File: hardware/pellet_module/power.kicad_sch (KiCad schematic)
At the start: 28 parts, among them J22 Barrel_Jack_Switch, U8 TPS561201, U9 TPS565208

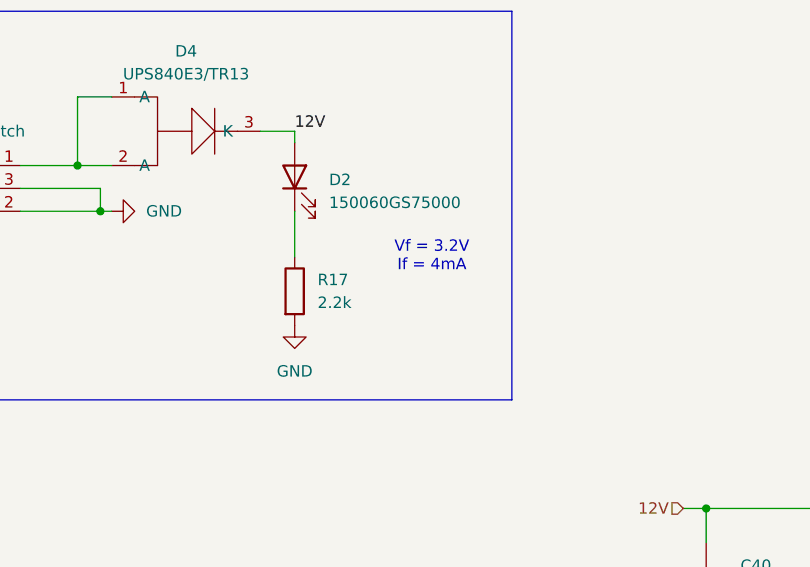
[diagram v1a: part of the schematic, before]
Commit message: reduce power LED brightness
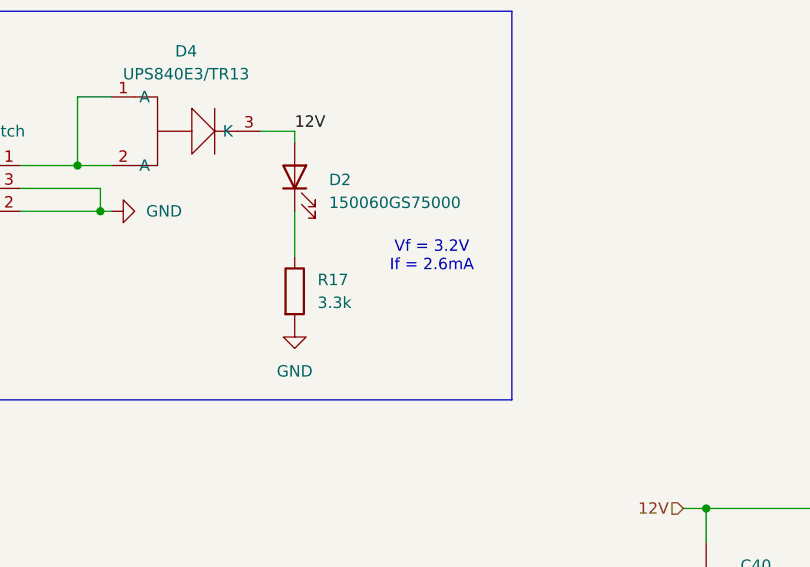
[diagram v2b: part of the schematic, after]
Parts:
- R17: value 2.2k -> 3.3k; LCSC C4190 -> C22978; MPN 0603WAF2201T5E -> 0603WAF3301T5E
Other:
- note added: "Vf = 3.2V If = 2.6mA"
- note removed: "Vf = 3.2V If = 4mA"
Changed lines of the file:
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@@
 		)
 	)
-	(text "Vf = 3.2V\nIf = 4mA"
+	(text "Vf = 3.2V\nIf = 2.6mA"
 		(exclude_from_sim no)
 		(at 78.74 45.72 0)
@@
 			)
 		)
-		(property "Value" "2.2k"
+		(property "Value" "3.3k"
 			(at 66.04 50.7999 0)
 			(effects
@@
 			)
 		)
-		(property "MPN" "0603WAF2201T5E"
+		(property "MPN" "0603WAF3301T5E"
 			(at 63.5 49.53 0)
 			(effects
@@
 			)
 		)
-		(property "LCSC" "C4190"
+		(property "LCSC" "C22978"
 			(at 63.5 49.53 0)
 			(effects

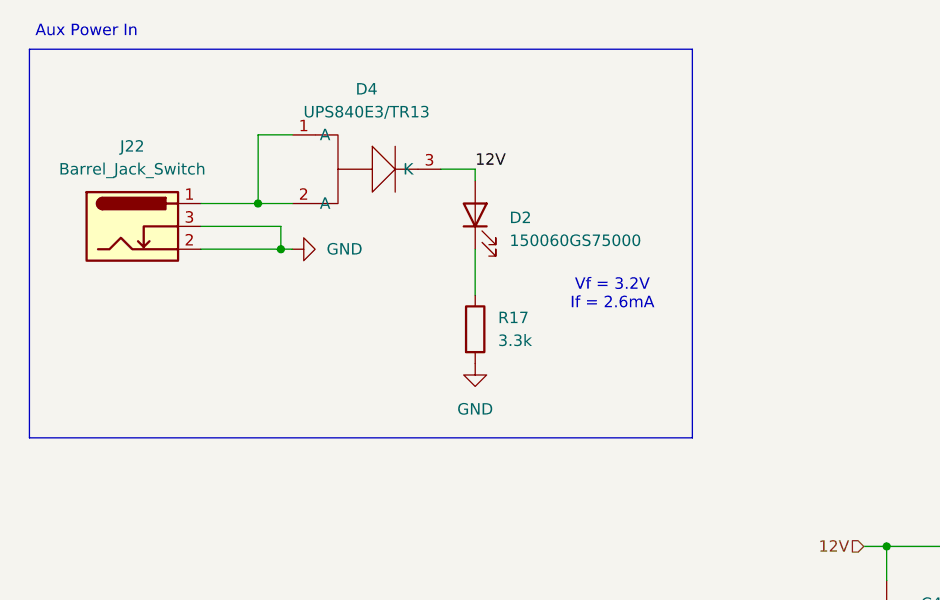
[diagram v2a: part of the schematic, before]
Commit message: add test points to schematic
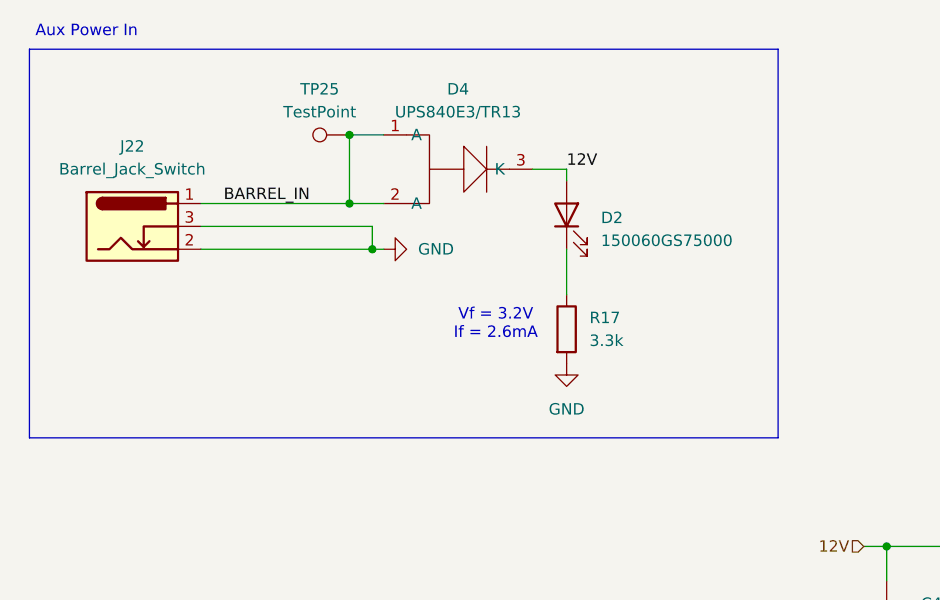
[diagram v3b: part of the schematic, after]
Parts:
- added TP25: TestPoint, TestPoint:TestPoint_Pad_1.0x1.0mm, symbol Connector:TestPoint
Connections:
- net BARREL_IN: now reaches D4.1 (A), D4.2 (A), J22.1
- net BARREL_IN: now also TP25.1
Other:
- moved on the sheet: D2, D4, R17
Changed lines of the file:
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@@
 	)
 	(junction
-		(at 41.91 40.64)
+		(at 52.07 40.64)
 		(diameter 0)
 		(color 0 0 0 0)
@@
 	)
 	(junction
+		(at 49.53 27.94)
+		(diameter 0)
+		(color 0 0 0 0)
+	)
+	(junction
 		(at 69.85 152.4)
 		(diameter 0)
@@
 	)
 	(junction
-		(at 39.37 35.56)
+		(at 49.53 35.56)
 		(diameter 0)
 		(color 0 0 0 0)
@@
 	(wire
 		(pts
-			(xy 43.18 40.64) (xy 41.91 40.64)
+			(xy 53.34 40.64) (xy 52.07 40.64)
 		)
 		(stroke
@@
 	(wire
 		(pts
-			(xy 59.69 31.75) (xy 63.5 31.75)
+			(xy 69.85 31.75) (xy 73.66 31.75)
 		)
 		(stroke
@@
 	(wire
 		(pts
-			(xy 41.91 40.64) (xy 33.02 40.64)
+			(xy 52.07 40.64) (xy 33.02 40.64)
 		)
 		(stroke
@@
 	(wire
 		(pts
-			(xy 43.18 27.94) (xy 39.37 27.94)
+			(xy 53.34 27.94) (xy 49.53 27.94)
 		)
 		(stroke
@@
 	(wire
 		(pts
-			(xy 33.02 38.1) (xy 41.91 38.1)
+			(xy 33.02 38.1) (xy 52.07 38.1)
 		)
 		(stroke
@@
 	(wire
 		(pts
-			(xy 39.37 27.94) (xy 39.37 35.56)
+			(xy 49.53 27.94) (xy 49.53 35.56)
 		)
 		(stroke
@@
 	(wire
 		(pts
-			(xy 41.91 38.1) (xy 41.91 40.64)
+			(xy 52.07 38.1) (xy 52.07 40.64)
 		)
 		(stroke
@@
 	(wire
 		(pts
-			(xy 33.02 35.56) (xy 39.37 35.56)
+			(xy 33.02 35.56) (xy 49.53 35.56)
 		)
 		(stroke
@@
 	(wire
 		(pts
-			(xy 39.37 35.56) (xy 43.18 35.56)
+			(xy 49.53 35.56) (xy 53.34 35.56)
 		)
 		(stroke
@@
 	(wire
 		(pts
-			(xy 63.5 40.64) (xy 63.5 45.72)
+			(xy 73.66 40.64) (xy 73.66 45.72)
 		)
 		(stroke
@@
 	(wire
 		(pts
-			(xy 63.5 31.75) (xy 63.5 33.02)
+			(xy 73.66 31.75) (xy 73.66 33.02)
 		)
 		(stroke
@@
 	(rectangle
 		(start 13.97 18.415)
-		(end 87.63 61.595)
+		(end 97.155 61.595)
 		(stroke
 			(width 0)
@@
 	(text "Vf = 3.2V\nIf = 2.6mA"
 		(exclude_from_sim no)
-		(at 78.74 45.72 0)
+		(at 65.786 49.022 0)
 		(effects
 			(font
@@
 	)
 	(label "12V"
-		(at 63.5 31.75 0)
+		(at 73.66 31.75 0)
 		(fields_autoplaced yes)
 		(effects
@@
 		)
 	)
+	(label "BARREL_IN"
+		(at 35.56 35.56 0)
+		(fields_autoplaced yes)
+		(effects
+			(font
+				(size 1.27 1.27)
+			)
+			(justify left bottom)
+		)
+	)
 	(label "12V"
 		(at 48.26 152.4 0)
@@
 	(symbol
 		(lib_id "Device:R")
-		(at 63.5 49.53 0)
+		(at 73.66 49.53 0)
 		(unit 1)
 		(exclude_from_sim no)
@@
 		(fields_autoplaced yes)
 		(property "Reference" "R17"
-			(at 66.04 48.2599 0)
+			(at 76.2 48.2599 0)
 			(effects
 				(font
@@
 		)
 		(property "Value" "3.3k"
-			(at 66.04 50.7999 0)
+			(at 76.2 50.7999 0)
 			(effects
 				(font
@@
 		)
 		(property "Footprint" "Resistor_SMD:R_0603_1608Metric"
-			(at 61.722 49.53 90)
+			(at 71.882 49.53 90)
 			(effects
 				(font
@@
 		)
 		(property "Datasheet" "~"
-			(at 63.5 49.53 0)
+			(at 73.66 49.53 0)
 			(effects
 				(font
@@
 		)
 		(property "Description" "Resistor"
-			(at 63.5 49.53 0)
+			(at 73.66 49.53 0)
 			(effects
 				(font
@@
 		)
 		(property "MPN" "0603WAF3301T5E"
-			(at 63.5 49.53 0)
+			(at 73.66 49.53 0)
 			(effects
 				(font
@@
 		)
 		(property "LCSC" "C22978"
-			(at 63.5 49.53 0)
+			(at 73.66 49.53 0)
 			(effects
 				(font
@@
 	(symbol
 		(lib_id "Connector:TestPoint")
+		(at 49.53 27.94 90)
+		(unit 1)
+		(exclude_from_sim no)
+		(in_bom no)
+		(on_board yes)
+		(dnp no)
+		(fields_autoplaced yes)
+		(property "Reference" "TP25"
+			(at 46.228 22.86 90)
+			(effects
+				(font
+					(size 1.27 1.27)
+				)
+			)
+		)
+		(property "Value" "TestPoint"
+			(at 46.228 25.4 90)
+			(effects
+				(font
+					(size 1.27 1.27)
+				)
+			)
+		)
+		(property "Footprint" "TestPoint:TestPoint_Pad_1.0x1.0mm"
+			(at 49.53 22.86 0)
+			(effects
+				(font
+					(size 1.27 1.27)
+				)
+				(hide yes)
+			)
+		)
+		(property "Datasheet" "~"
+			(at 49.53 22.86 0)
+			(effects
+				(font
+					(size 1.27 1.27)
+				)
+				(hide yes)
+			)
+		)
+		(property "Description" "test point"
+			(at 49.53 27.94 0)
+			(effects
+				(font
+					(size 1.27 1.27)
+				)
+				(hide yes)
+			)
+		)
+		(pin "1"
+		)
+		(instances
+			(project "pellet"
+				(path "/48650363-a452-429d-997e-1ddabb69aad0/e506f537-c74c-4de3-bd3a-98b1a75d4ef5"
+					(reference "TP25")
+					(unit 1)
+				)
+			)
+		)
+	)
+	(symbol
+		(lib_id "Connector:TestPoint")
 		(at 242.57 128.27 90)
 		(unit 1)
@@
 	(symbol
 		(lib_id "Device:LED")
-		(at 63.5 36.83 90)
+		(at 73.66 36.83 90)
 		(unit 1)
 		(exclude_from_sim no)
@@
 		(fields_autoplaced yes)
 		(property "Reference" "D2"
-			(at 67.31 37.1474 90)
+			(at 77.47 37.1474 90)
 			(effects
 				(font
@@
 		)
 		(property "Value" "150060GS75000"
-			(at 67.31 39.6874 90)
+			(at 77.47 39.6874 90)
 			(effects
 				(font
@@
 		)
 		(property "Footprint" "Diode_SMD:D_0603_1608Metric"
-			(at 63.5 36.83 0)
+			(at 73.66 36.83 0)
 			(effects
 				(font
@@
 		)
 		(property "Datasheet" "~"
-			(at 63.5 36.83 0)
+			(at 73.66 36.83 0)
 			(effects
 				(font
@@
 		)
 		(property "Description" "Light emitting diode"
-			(at 63.5 36.83 0)
+			(at 73.66 36.83 0)
 			(effects
 				(font
@@
 		)
 		(property "MPN" "150060GS75000"
-			(at 63.5 36.83 0)
+			(at 73.66 36.83 0)
 			(effects
 				(font
@@
 		)
 		(property "LCSC" "C5252984"
-			(at 63.5 36.83 0)
+			(at 73.66 36.83 0)
 			(effects
 				(font
@@
 	(symbol
 		(lib_id "power:GND")
-		(at 63.5 53.34 0)
+		(at 73.66 53.34 0)
 		(unit 1)
 		(exclude_from_sim no)
@@
 		(fields_autoplaced yes)
 		(property "Reference" "#PWR010"
-			(at 63.5 59.69 0)
+			(at 73.66 59.69 0)
 			(effects
 				(font
@@
 		)
 		(property "Value" "GND"
-			(at 63.5 58.42 0)
+			(at 73.66 58.42 0)
 			(effects
 				(font
@@
 		)
 		(property "Footprint" ""
-			(at 63.5 53.34 0)
+			(at 73.66 53.34 0)
 			(effects
 				(font
@@
 		)
 		(property "Datasheet" ""
-			(at 63.5 53.34 0)
+			(at 73.66 53.34 0)
 			(effects
 				(font
@@
 		)
 		(property "Description" "Power symbol creates a global label with name \"GND\" , ground"
-			(at 63.5 53.34 0)
+			(at 73.66 53.34 0)
 			(effects
 				(font
@@
 	(symbol
 		(lib_id "power:GND")
-		(at 43.18 40.64 90)
+		(at 53.34 40.64 90)
 		(unit 1)
 		(exclude_from_sim no)
@@
 		(fields_autoplaced yes)
 		(property "Reference" "#PWR080"
-			(at 49.53 40.64 0)
+			(at 59.69 40.64 0)
 			(effects
 				(font
@@
 		)
 		(property "Value" "GND"
-			(at 46.99 40.6399 90)
+			(at 57.15 40.6399 90)
 			(effects
 				(font
@@
 		)
 		(property "Footprint" ""
-			(at 43.18 40.64 0)
+			(at 53.34 40.64 0)
 			(effects
 				(font
@@
 		)
 		(property "Datasheet" ""
-			(at 43.18 40.64 0)
+			(at 53.34 40.64 0)
 			(effects
 				(font
@@
 		)
 		(property "Description" "Power symbol creates a global label with name \"GND\" , ground"
-			(at 43.18 40.64 0)
+			(at 53.34 40.64 0)
 			(effects
 				(font
@@
 	(symbol
 		(lib_id "Leaf_Diode:Diode_123")
-		(at 52.07 29.21 180)
+		(at 62.23 29.21 180)
 		(unit 1)
 		(exclude_from_sim no)
@@
 		(fields_autoplaced yes)
 		(property "Reference" "D4"
-			(at 51.435 22.86 0)
+			(at 61.595 22.86 0)
 			(effects
 				(font
@@
 		)
 		(property "Value" "UPS840E3/TR13"
-			(at 51.435 25.4 0)
+			(at 61.595 25.4 0)
 			(effects
 				(font
@@
 		)
 		(property "Footprint" "Leaf_Diode:POWERMITE3_MCH"
-			(at 52.07 29.21 0)
+			(at 62.23 29.21 0)
 			(effects
 				(font
@@
 		)
 		(property "Datasheet" "~"
-			(at 52.07 29.21 0)
+			(at 62.23 29.21 0)
 			(effects
 				(font
@@
 		)
 		(property "Description" "Diode"
-			(at 52.07 29.21 0)
+			(at 62.23 29.21 0)
 			(effects
 				(font
@@
 		)
 		(property "Sim.Device" "D"
-			(at 52.07 29.21 0)
+			(at 62.23 29.21 0)
 			(effects
 				(font
@@
 		)
 		(property "Sim.Pins" "1=K 2=A"
-			(at 52.07 29.21 0)
+			(at 62.23 29.21 0)
 			(effects
 				(font
@@
 		)
 		(property "MPN" "UPS840E3/TR13"
-			(at 52.07 29.21 0)
+			(at 62.23 29.21 0)
 			(effects
 				(font
@@
 		)
 		(property "LCSC" "C3758317"
-			(at 52.07 29.21 0)
+			(at 62.23 29.21 0)
 			(effects
 				(font
